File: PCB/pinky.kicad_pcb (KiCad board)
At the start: 2 copper layers, 54 parts, among them SW10 Switch, SW11 Switch, SW12 Switch, SW13 Switch, SW14 Switch, SW15 Switch, SW16 Switch, SW17 Switch, SW18 Switch, SW2 Switch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

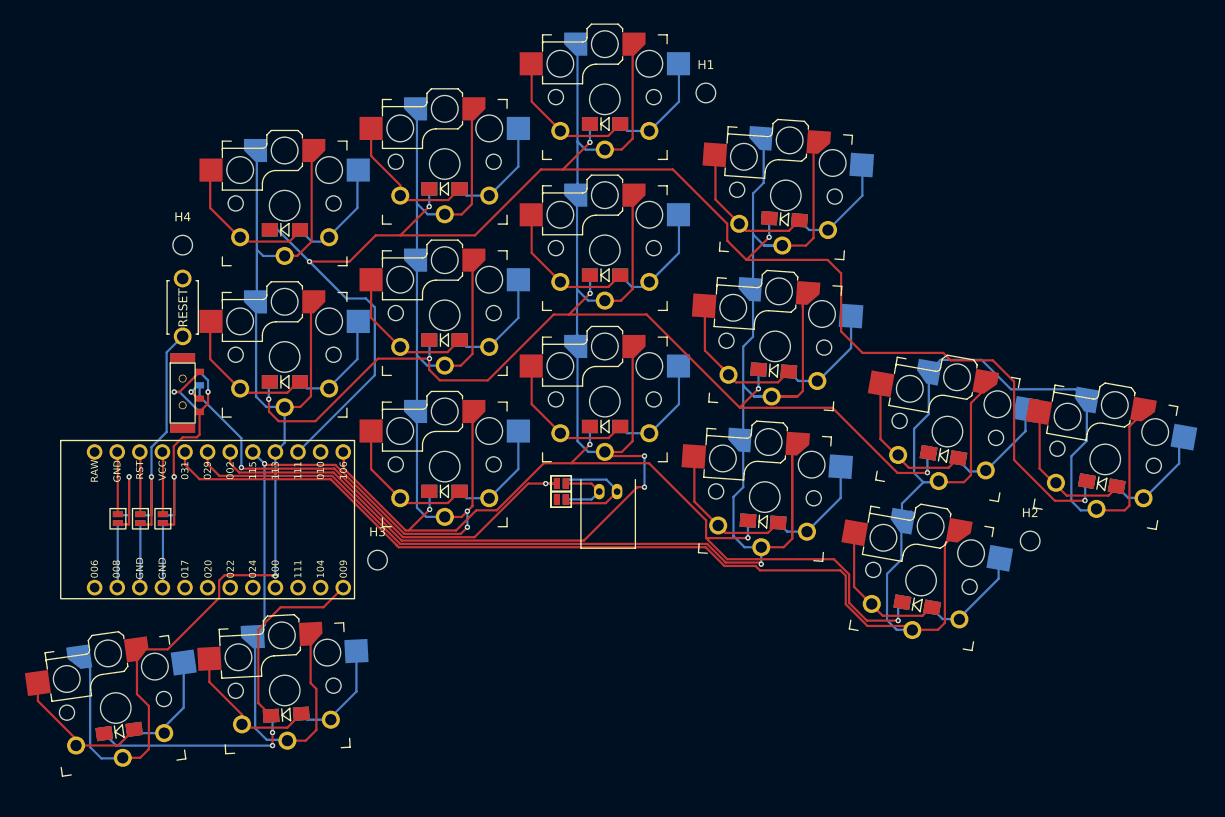
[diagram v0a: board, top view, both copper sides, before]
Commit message: An outline of the cuts added
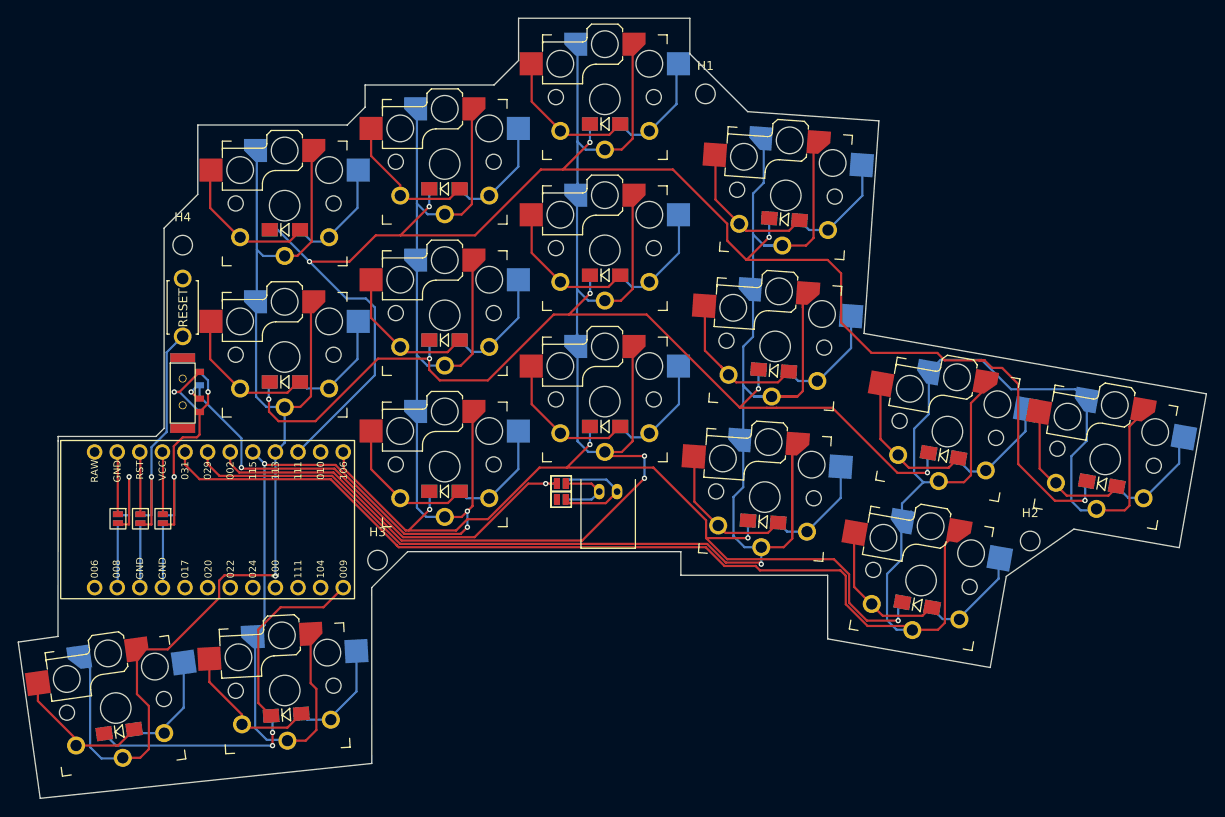
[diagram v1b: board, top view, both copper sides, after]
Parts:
- moved H1 0.11 mm to (164.2, 58.0)
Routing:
- net col_C: track 160.6 -> 160.0 mm
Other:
- board outline added: 133.5 x 87.7 mm

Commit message: Footprints and scheme update
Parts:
- JP2, JP3, JP4: value Jumper -> SDA
